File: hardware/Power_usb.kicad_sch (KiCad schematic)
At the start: 7 parts

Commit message: layout starte but i want to play codename
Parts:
- renumbered TP27 to TP25, TP28 to TP26, TP29 to TP27, TP25 to TP28, TP26 to TP29
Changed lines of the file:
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@@
 		(dnp no)
 		(fields_autoplaced yes)
-		(property "Reference" "#PWR026"
+		(property "Reference" "#PWR027"
 			(at 139.7 66.04 0)
 			(hide yes)
@@
 			(project "PS-PowerDistributionUnit"
 				(path "/eb16378f-e371-46a9-bfab-b0d9404d0362/e5e6ee2e-1d09-4fff-9eef-bc055f220fc3"
-					(reference "#PWR026")
+					(reference "#PWR027")
 					(unit 1)
 				)
@@
 		(in_pos_files yes)
 		(dnp no)
-		(property "Reference" "TP29"
+		(property "Reference" "TP27"
 			(at 156.845 121.7929 0)
 			(hide yes)
@@
 			(project "PS-PowerDistributionUnit"
 				(path "/eb16378f-e371-46a9-bfab-b0d9404d0362/e5e6ee2e-1d09-4fff-9eef-bc055f220fc3"
-					(reference "TP29")
+					(reference "TP27")
 					(unit 1)
 				)
@@
 		(in_pos_files yes)
 		(dnp no)
-		(property "Reference" "TP26"
+		(property "Reference" "TP29"
 			(at 207.645 46.99 0)
 			(show_name no)
@@
 			(project "PS-PowerDistributionUnit"
 				(path "/eb16378f-e371-46a9-bfab-b0d9404d0362/e5e6ee2e-1d09-4fff-9eef-bc055f220fc3"
-					(reference "TP26")
+					(reference "TP29")
 					(unit 1)
 				)
@@
 		(in_pos_files yes)
 		(dnp no)
-		(property "Reference" "TP28"
+		(property "Reference" "TP26"
 			(at 142.875 121.7929 0)
 			(hide yes)
@@
 			(project "PS-PowerDistributionUnit"
 				(path "/eb16378f-e371-46a9-bfab-b0d9404d0362/e5e6ee2e-1d09-4fff-9eef-bc055f220fc3"
-					(reference "TP28")
+					(reference "TP26")
 					(unit 1)
 				)
@@
 		(dnp no)
 		(fields_autoplaced yes)
-		(property "Reference" "#PWR0139"
+		(property "Reference" "#PWR028"
 			(at 160.655 147.955 0)
 			(hide yes)
@@
 			(project "PS-PowerDistributionUnit"
 				(path "/eb16378f-e371-46a9-bfab-b0d9404d0362/e5e6ee2e-1d09-4fff-9eef-bc055f220fc3"
-					(reference "#PWR0139")
+					(reference "#PWR028")
 					(unit 1)
 				)
@@
 		(dnp no)
 		(fields_autoplaced yes)
-		(property "Reference" "#PWR013"
+		(property "Reference" "#PWR025"
 			(at 93.345 147.32 0)
 			(hide yes)
@@
 			(project "PS-PowerDistributionUnit"
 				(path "/eb16378f-e371-46a9-bfab-b0d9404d0362/e5e6ee2e-1d09-4fff-9eef-bc055f220fc3"
-					(reference "#PWR013")
+					(reference "#PWR025")
 					(unit 1)
 				)
@@
 		(in_pos_files yes)
 		(dnp no)
-		(property "Reference" "TP25"
+		(property "Reference" "TP28"
 			(at 177.8 46.99 0)
 			(show_name no)
@@
 			(project "PS-PowerDistributionUnit"
 				(path "/eb16378f-e371-46a9-bfab-b0d9404d0362/e5e6ee2e-1d09-4fff-9eef-bc055f220fc3"
-					(reference "TP25")
+					(reference "TP28")
 					(unit 1)
 				)
@@
 		(in_pos_files yes)
 		(dnp no)
-		(property "Reference" "TP27"
+		(property "Reference" "TP25"
 			(at 136.525 117.9829 0)
 			(hide yes)
@@
 			(project "PS-PowerDistributionUnit"
 				(path "/eb16378f-e371-46a9-bfab-b0d9404d0362/e5e6ee2e-1d09-4fff-9eef-bc055f220fc3"
-					(reference "TP27")
+					(reference "TP25")
 					(unit 1)
 				)
@@
 		(dnp no)
 		(fields_autoplaced yes)
-		(property "Reference" "#PWR027"
+		(property "Reference" "#PWR029"
 			(at 187.325 65.405 0)
 			(hide yes)
@@
 			(project "PS-PowerDistributionUnit"
 				(path "/eb16378f-e371-46a9-bfab-b0d9404d0362/e5e6ee2e-1d09-4fff-9eef-bc055f220fc3"
-					(reference "#PWR027")
+					(reference "#PWR029")
 					(unit 1)
 				)
@@
 		(in_pos_files yes)
 		(dnp no)
-		(property "Reference" "#PWR025"
+		(property "Reference" "#PWR026"
 			(at 100.965 67.31 0)
 			(hide yes)
@@
 			(project "PS-PowerDistributionUnit"
 				(path "/eb16378f-e371-46a9-bfab-b0d9404d0362/e5e6ee2e-1d09-4fff-9eef-bc055f220fc3"
-					(reference "#PWR025")
-					(unit 1)
-				)
+					(reference "#PWR026")
+					(unit 1)
+				)

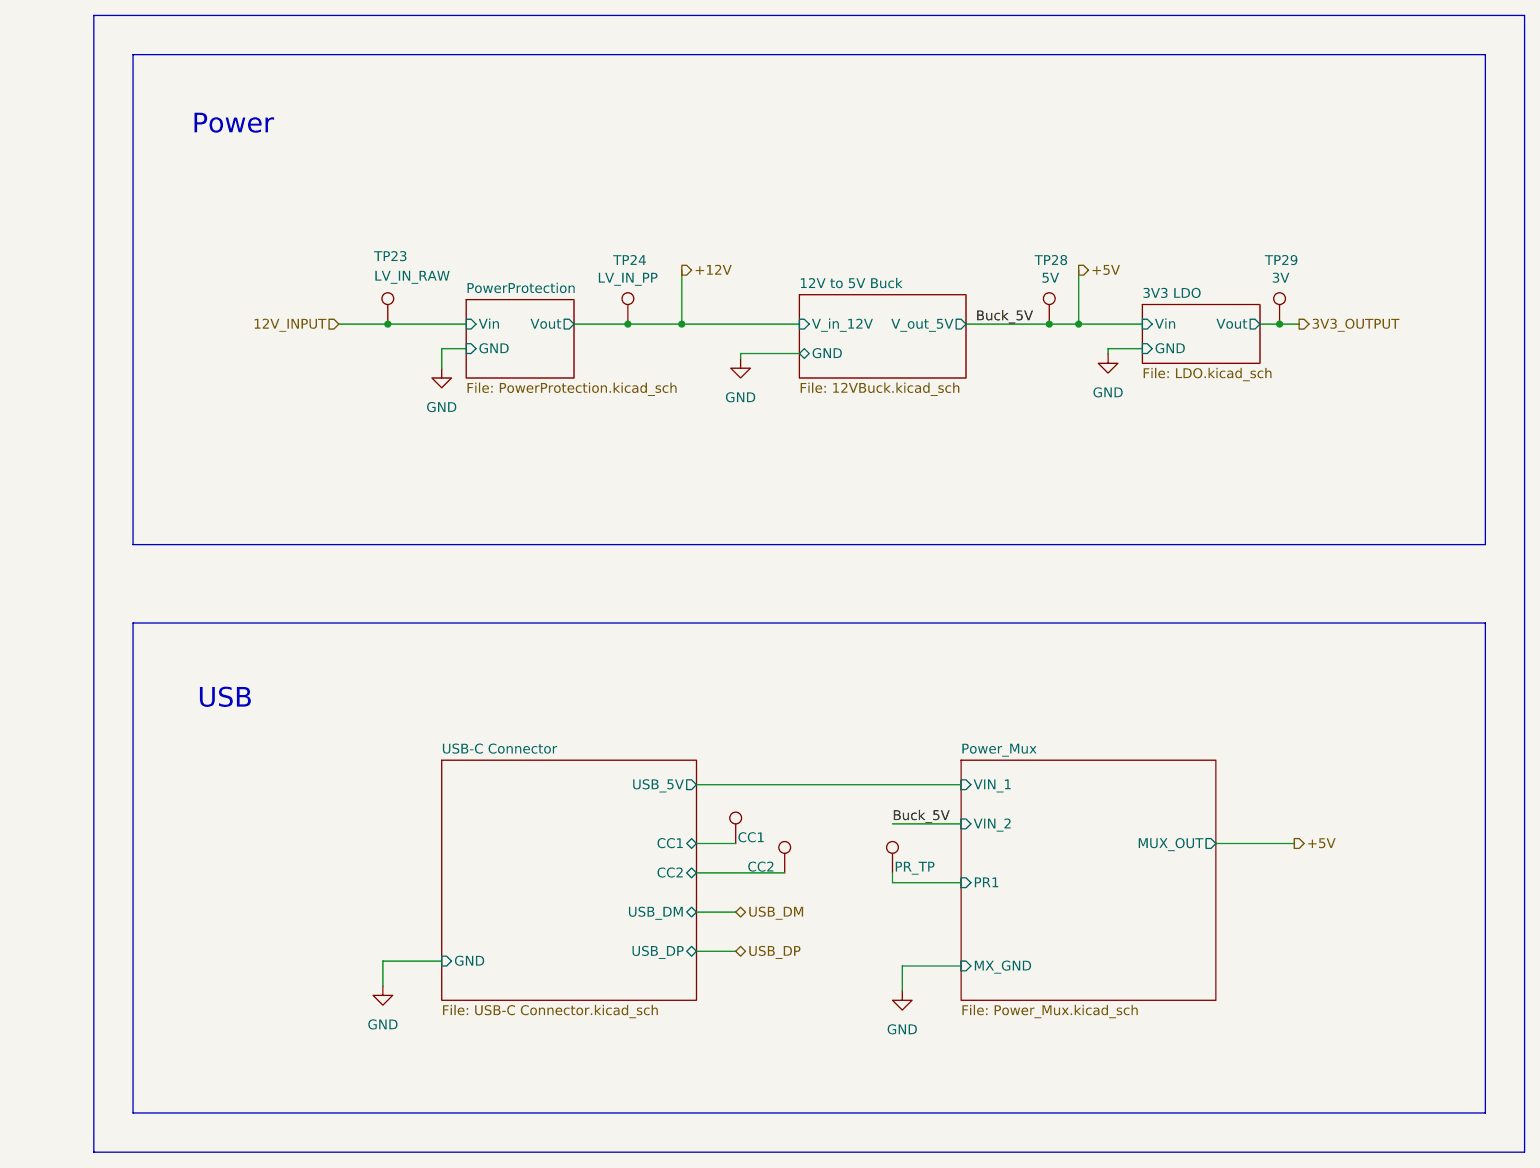
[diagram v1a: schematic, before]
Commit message: fixed usb and power
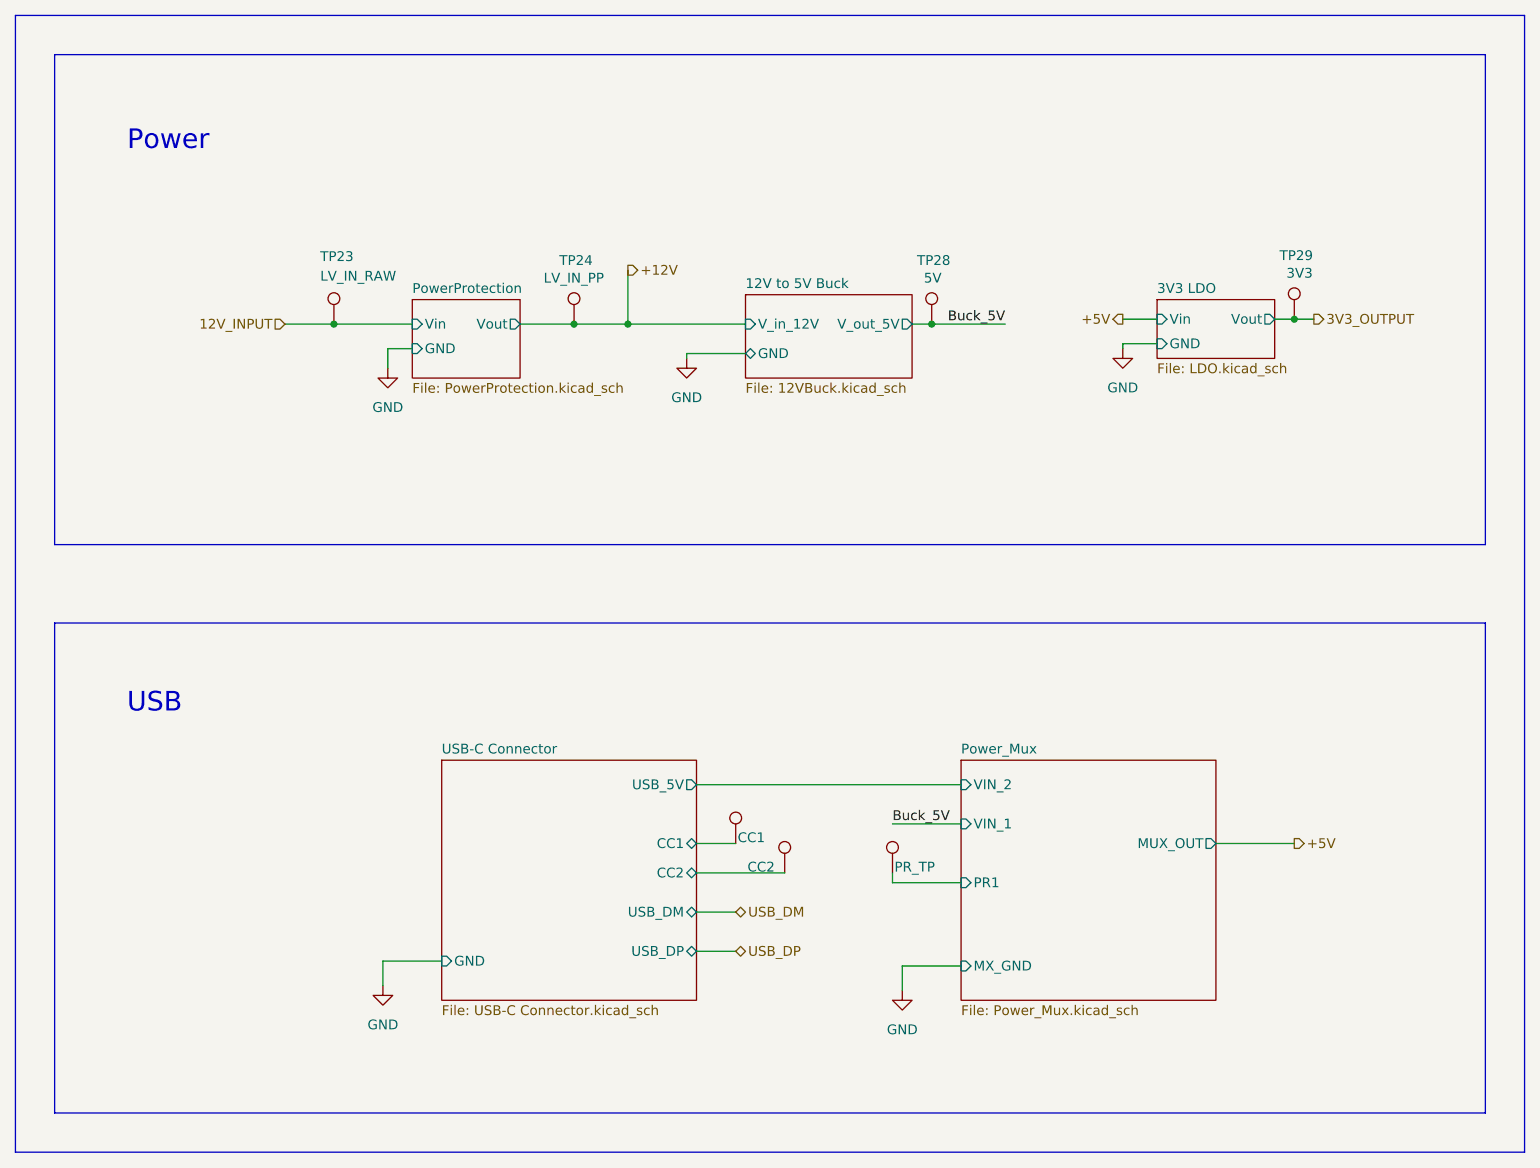
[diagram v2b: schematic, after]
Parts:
- TP29: value 3V -> 3V3
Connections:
- net +5V: no longer TP28.1
- new net Buck_5V: TP28.1
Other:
- moved on the sheet: TP23, TP24, TP29

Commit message: done w HSS and PP
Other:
- removed sheet 12V to 5V Buck
- added sheet 12VBuck (12VBuck.kicad_sch)
- moved on the sheet: TP28
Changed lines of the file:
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@@
 	)
 	(junction
-		(at 164.465 55.245)
+		(at 168.275 59.69)
 		(diameter 0)
 		(color 0 0 0 0)
@@
 	(wire
 		(pts
-			(xy 161.925 55.245) (xy 164.465 55.245)
-		)
-		(stroke
-			(width 0)
-			(type default)
-		)
-	)
-	(wire
-		(pts
 			(xy 125.095 48.26) (xy 125.095 55.245)
 		)
@@
 	(wire
 		(pts
-			(xy 132.715 59.69) (xy 132.715 59.055)
-		)
-		(stroke
-			(width 0)
-			(type default)
-		)
-	)
-	(wire
-		(pts
-			(xy 132.715 59.055) (xy 140.335 59.055)
+			(xy 136.525 64.135) (xy 136.525 63.5)
+		)
+		(stroke
+			(width 0)
+			(type default)
+		)
+	)
+	(wire
+		(pts
+			(xy 136.525 63.5) (xy 144.145 63.5)
 		)
 		(stroke
@@
 	(wire
 		(pts
-			(xy 125.095 55.245) (xy 140.335 55.245)
-		)
-		(stroke
-			(width 0)
-			(type default)
-		)
-	)
-	(wire
-		(pts
-			(xy 164.465 55.245) (xy 173.99 55.245)
+			(xy 125.095 55.245) (xy 144.145 55.245)
+		)
+		(stroke
+			(width 0)
+			(type default)
+		)
+	)
+	(wire
+		(pts
+			(xy 168.275 59.69) (xy 177.8 59.69)
 		)
 		(stroke
@@
 	(wire
 		(pts
+			(xy 164.465 59.69) (xy 168.275 59.69)
+		)
+		(stroke
+			(width 0)
+			(type default)
+		)
+	)
+	(wire
+		(pts
 			(xy 80.645 55.245) (xy 86.995 55.245)
 		)
@@
 	)
 	(label "Buck_5V"
-		(at 173.99 55.245 180)
+		(at 177.8 59.69 180)
 		(effects
 			(font
@@
 	(symbol
 		(lib_id "power:GND")
-		(at 132.715 59.69 0)
+		(at 136.525 64.135 0)
 		(unit 1)
 		(body_style 1)
@@
 		(fields_autoplaced yes)
 		(property "Reference" "#PWR027"
-			(at 132.715 66.04 0)
+			(at 136.525 70.485 0)
 			(hide yes)
 			(show_name no)
@@
 		)
 		(property "Value" "GND"
-			(at 132.715 64.77 0)
+			(at 136.525 69.215 0)
 			(show_name no)
 			(do_not_autoplace no)
@@
 		)
 		(property "Footprint" ""
-			(at 132.715 59.69 0)
+			(at 136.525 64.135 0)
 			(hide yes)
 			(show_name no)
@@
 		)
 		(property "Datasheet" ""
-			(at 132.715 59.69 0)
+			(at 136.525 64.135 0)
 			(hide yes)
 			(show_name no)
@@
 		)
 		(property "Description" "Power symbol creates a global label with name \"GND\" , ground"
-			(at 132.715 59.69 0)
+			(at 136.525 64.135 0)
 			(hide yes)
 			(show_name no)
@@
 	(symbol
 		(lib_id "Connector:TestPoint")
-		(at 164.465 55.245 0)
+		(at 168.275 59.69 0)
 		(unit 1)
 		(body_style 1)
@@
 		(dnp no)
 		(property "Reference" "TP28"
-			(at 162.56 46.99 0)
+			(at 166.37 51.435 0)
 			(show_name no)
 			(do_not_autoplace no)
@@
 		)
 		(property "Value" "5V"
-			(at 163.449 49.276 0)
+			(at 167.259 53.721 0)
 			(show_name no)
 			(do_not_autoplace no)
@@
 		)
 		(property "Footprint" "TestPoint:TestPoint_THTPad_D3.0mm_Drill1.5mm"
-			(at 169.545 55.245 0)
+			(at 173.355 59.69 0)
 			(hide yes)
 			(show_name no)
@@
 		)
 		(property "Datasheet" ""
-			(at 169.545 55.245 0)
+			(at 173.355 59.69 0)
 			(hide yes)
 			(show_name no)
@@
 		)
 		(property "Description" "test point"
-			(at 164.465 55.245 0)
+			(at 168.275 59.69 0)
 			(hide yes)
 			(show_name no)
@@
 	)
 	(sheet
-		(at 140.335 51.435)
-		(size 21.59 10.795)
-		(exclude_from_sim no)
-		(in_bom yes)
-		(on_board yes)
-		(dnp no)
-		(fields_autoplaced yes)
-		(stroke
-			(width 0.1524)
-			(type solid)
-		)
-		(fill
-			(color 0 0 0 0)
-		)
-		(property "Sheetname" "12V to 5V Buck"
-			(at 140.335 50.7234 0)
-			(show_name no)
-			(do_not_autoplace no)
-			(effects
-				(font
-					(size 1.27 1.27)
-				)
-				(justify left bottom)
-			)
-		)
-		(property "Sheetfile" "12VBuck.kicad_sch"
-			(at 140.335 62.8146 0)
-			(show_name no)
-			(do_not_autoplace no)
-			(effects
-				(font
-					(size 1.27 1.27)
-				)
-				(justify left top)
-			)
-		)
-		(pin "GND" bidirectional
-			(at 140.335 59.055 180)
-			(effects
-				(font
-					(size 1.27 1.27)
-				)
-				(justify left)
-			)
-		)
-		(pin "V_in_12V" input
-			(at 140.335 55.245 180)
-			(effects
-				(font
-					(size 1.27 1.27)
-				)
-				(justify left)
-			)
-		)
-		(pin "V_out_5V" output
-			(at 161.925 55.245 0)
-			(effects
-				(font
-					(size 1.27 1.27)
-				)
-				(justify right)
-			)
-		)
-		(instances
-			(project "PS-PowerDistributionUnit"
-				(path "/eb16378f-e371-46a9-bfab-b0d9404d0362/e5e6ee2e-1d09-4fff-9eef-bc055f220fc3"
-					(page "16")
-				)
-			)
-		)
-	)
-	(sheet
 		(at 97.155 52.07)
 		(size 13.97 10.16)
@@
 				)
 			)
+		)
+	)
+	(sheet
+		(at 144.145 50.8)
+		(size 20.32 20.32)
+		(exclude_from_sim no)
+		(in_bom yes)
+		(on_board yes)
+		(dnp no)
+		(fields_autoplaced yes)
+		(stroke
+			(width 0.1524)
+			(type solid)
+		)
+		(fill
+			(color 0 0 0 0)
+		)
+		(property "Sheetname" "12VBuck"
+			(at 144.145 50.0884 0)
+			(show_name no)
+			(do_not_autoplace no)
+			(effects
+				(font
+					(size 1.27 1.27)
+				)
+				(justify left bottom)
+			)
+		)
+		(property "Sheetfile" "12VBuck.kicad_sch"
+			(at 144.145 71.7046 0)
+			(show_name no)
+			(do_not_autoplace no)
+			(effects
+				(font
+					(size 1.27 1.27)
+				)
+				(justify left top)
+			)
+		)
+		(pin "GND" bidirectional
+			(at 144.145 63.5 180)
+			(effects
+				(font
+					(size 1.27 1.27)
+				)
+				(justify left)
+			)
+		)
+		(pin "V_in_12V" input
+			(at 144.145 55.245 180)
+			(effects
+				(font
+					(size 1.27 1.27)
+				)
+				(justify left)
+			)
+		)
+		(pin "V_out_5V" output
+			(at 164.465 59.69 0)
+			(effects
+				(font
+					(size 1.27 1.27)
+				)
+				(justify right)
+			)
+		)
+		(instances
+			(project "PS-PowerDistributionUnit"
+				(path "/eb16378f-e371-46a9-bfab-b0d9404d0362/e5e6ee2e-1d09-4fff-9eef-bc055f220fc3"
+					(page "16")
+				)
+			)

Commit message: booooom not done tho
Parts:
- removed TP29: 3V3, TestPoint:TestPoint_THTPad_D3.0mm_Drill1.5mm, symbol Connector:TestPoint
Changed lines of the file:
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@@
-	)
-	(junction
-		(at 211.455 54.61)
-		(diameter 0)
-		(color 0 0 0 0)
 	)
 	(junction
@@
 	(wire
 		(pts
-			(xy 211.455 54.61) (xy 208.915 54.61)
+			(xy 208.915 54.61) (xy 213.995 54.61)
 		)
 		(stroke
@@
 		(pts
 			(xy 201.295 122.555) (xy 211.455 122.555)
-		)
-		(stroke
-			(width 0)
-			(type default)
-		)
-	)
-	(wire
-		(pts
-			(xy 213.995 54.61) (xy 211.455 54.61)
 		)
 		(stroke
@@
 					(unit 1)
 				)
-			)
-		)
-	)
-	(symbol
-		(lib_id "Connector:TestPoint")
-		(at 211.455 54.61 0)
-		(unit 1)
-		(body_style 1)
-		(exclude_from_sim no)
-		(in_bom yes)
-		(on_board yes)
-		(in_pos_files yes)
-		(dnp no)
-		(property "Reference" "TP29"
-			(at 209.55 46.355 0)
-			(show_name no)
-			(do_not_autoplace no)
-			(effects
-				(font
-					(size 1.27 1.27)
-				)
-				(justify left)
-			)
-		)
-		(property "Value" "3V3"
-			(at 210.439 48.641 0)
-			(show_name no)
-			(do_not_autoplace no)
-			(effects
-				(font
-					(size 1.27 1.27)
-				)
-				(justify left)
-			)
-		)
-		(property "Footprint" "TestPoint:TestPoint_THTPad_D3.0mm_Drill1.5mm"
-			(at 216.535 54.61 0)
-			(hide yes)
-			(show_name no)
-			(do_not_autoplace no)
-			(effects
-				(font
-					(size 1.27 1.27)
-				)
-			)
-		)
-		(property "Datasheet" ""
-			(at 216.535 54.61 0)
-			(hide yes)
-			(show_name no)
-			(do_not_autoplace no)
-			(effects
-				(font
-					(size 1.27 1.27)
-				)
-			)
-		)
-		(property "Description" "test point"
-			(at 211.455 54.61 0)
-			(hide yes)
-			(show_name no)
-			(do_not_autoplace no)
-			(effects
-				(font
-					(size 1.27 1.27)
-				)
-			)
-		)
-		(pin "1"
-		)
-		(instances
-			(project "PS-PowerDistributionUnit"
-				(path "/eb16378f-e371-46a9-bfab-b0d9404d0362/e5e6ee2e-1d09-4fff-9eef-bc055f220fc3"
-					(reference "TP29")
-					(unit 1)
-				)

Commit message: added pn
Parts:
- TP23: LCSC P/N C41426955 -> (none)
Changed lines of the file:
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@@
 			)
 		)
-		(property "LCSC P/N" "C41426955"
+		(property "LCSC P/N" ""
 			(at 86.995 55.245 0)
 			(hide yes)

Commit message: 411
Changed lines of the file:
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@@
+		)
+	)
+	(label "D-"
+		(at 135.255 136.525 0)
+		(effects
+			(font
+				(size 1.27 1.27)
+			)
+			(justify left bottom)
+		)
+	)
+	(label "D+"
+		(at 135.255 131.445 0)
+		(effects
+			(font
+				(size 1.27 1.27)
+			)
+			(justify left bottom)
 		)
 	)

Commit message: need to study matrices:
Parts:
- removed TP25: CC1, TestPoint:TestPoint_THTPad_D3.0mm_Drill1.5mm, symbol Connector:TestPoint
- removed TP26: CC2, TestPoint:TestPoint_THTPad_D3.0mm_Drill1.5mm, symbol Connector:TestPoint
- added R91: 0, Resistor_SMD:R_0603_1608Metric_Pad0.98x0.95mm_HandSolder, symbol Device:R
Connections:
- net +12V: now also R91.2
- net 12V_INPUT: now also R91.1
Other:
- sheet USB-C Connector ports: added none; removed CC1, CC2
- moved on the sheet: TP23, TP24

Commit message: back home
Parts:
- R91: now not fitted
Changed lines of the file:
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@@
 		(on_board yes)
 		(in_pos_files yes)
-		(dnp no)
+		(dnp yes)
 		(fields_autoplaced yes)
 		(property "Reference" "R91"
